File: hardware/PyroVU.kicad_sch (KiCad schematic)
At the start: 48 parts, among them IC1 TM1637__SOP_, J1 Screw_Terminal_01x05, J10 Screw_Terminal_01x09, J11 Screw_Terminal_01x09, J12 Screw_Terminal_01x09, J2 Screw_Terminal_01x02, J3 Conn_01x09_Pin, J4 Conn_01x02_Pin, J5 Conn_01x02_Pin, J6 Conn_01x02_Pin, J7 Screw_Terminal_01x09, J8 Screw_Terminal_01x09, J9 Screw_Terminal_01x09, U1 MAX31856, U3 MAX31865xTP

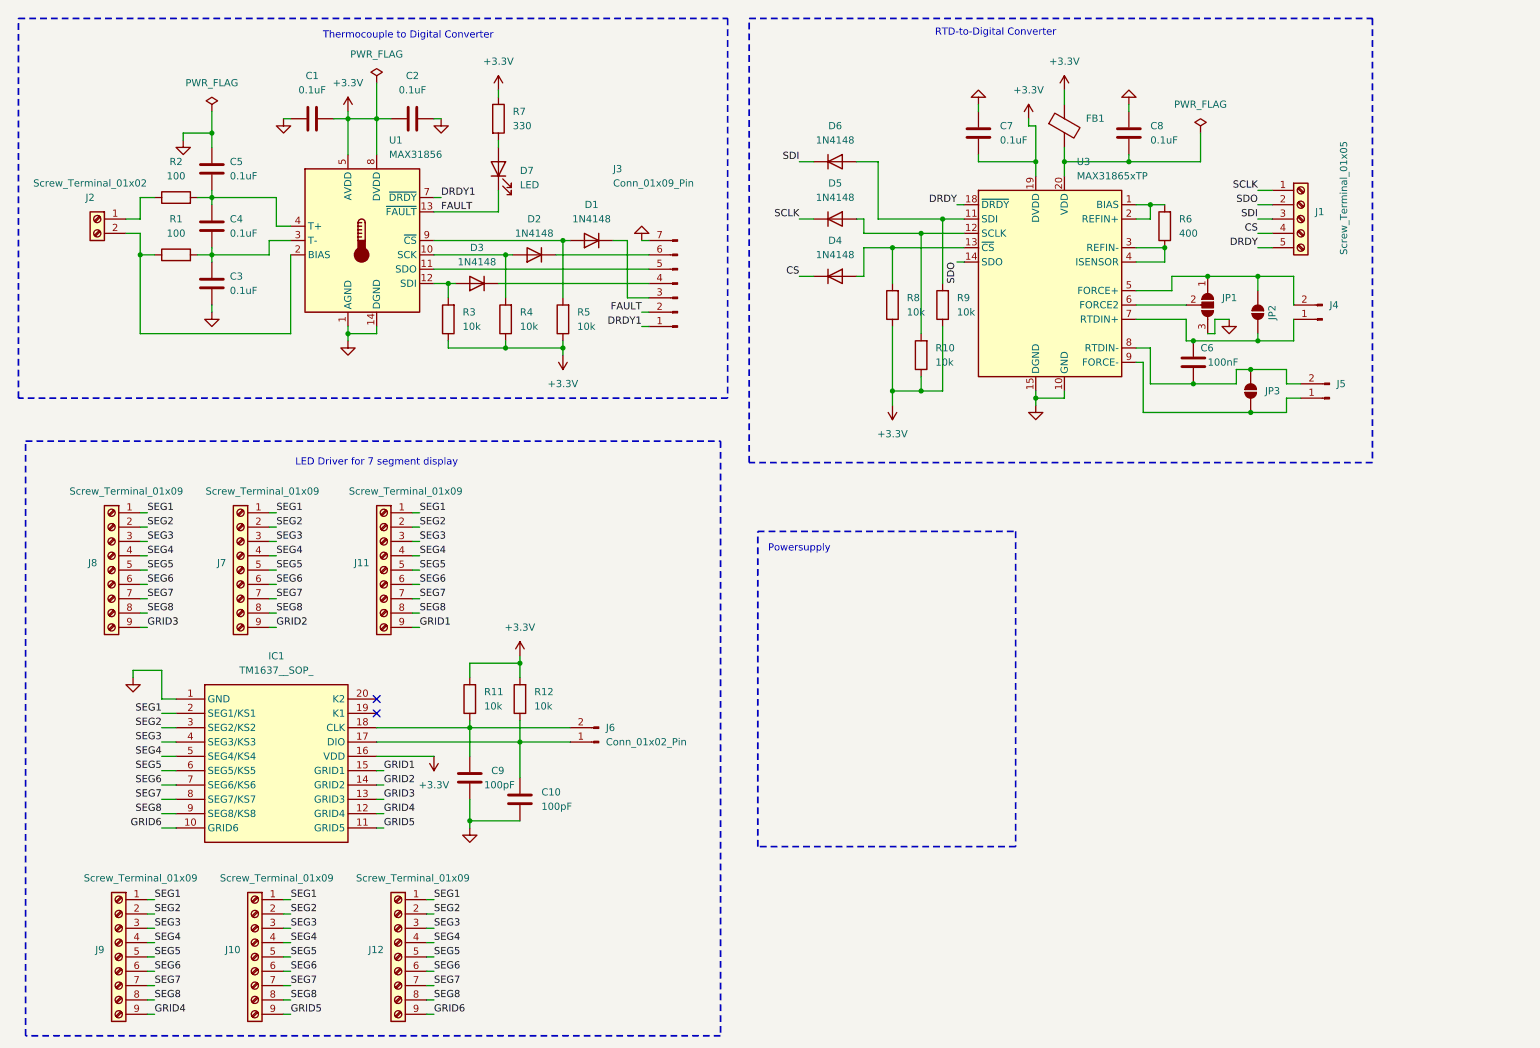
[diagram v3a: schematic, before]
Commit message: Updated the schematic and added 7seg display
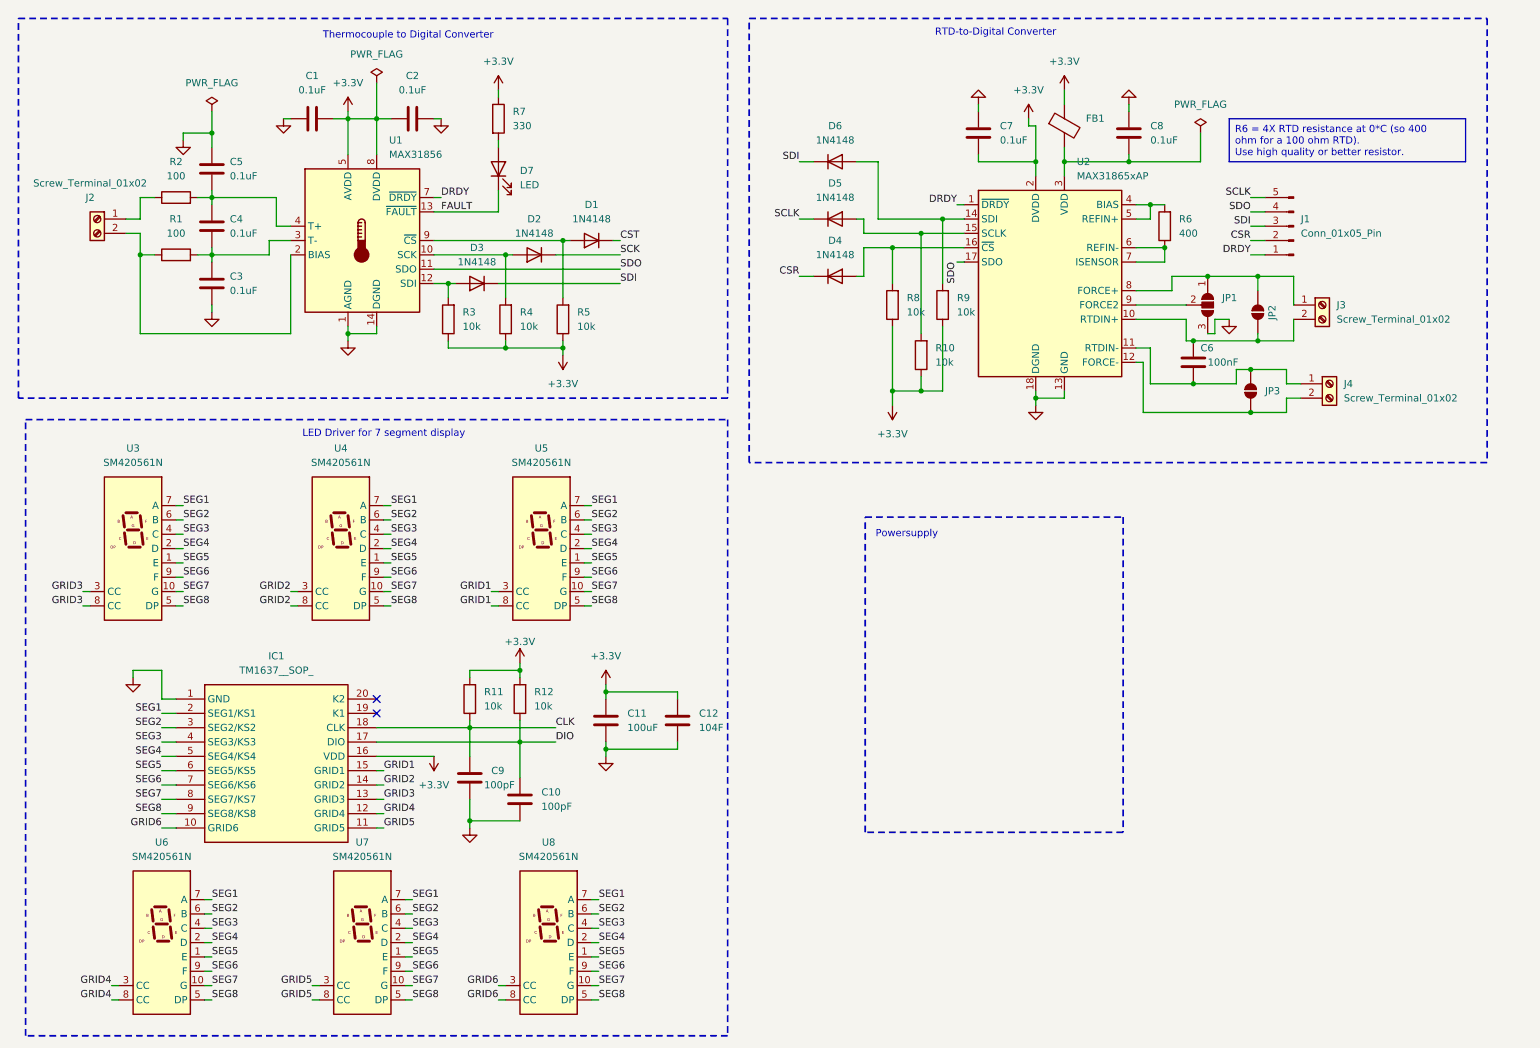
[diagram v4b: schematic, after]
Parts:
- removed J1: Screw_Terminal_01x05, TerminalBlock_Phoenix:TerminalBlock_Phoenix_MPT-0,5-5-2.54_1x05_P2.54mm_Horizontal, symbol Connector:Screw_Terminal_01x05
- removed J10, J11, J12, J7, J8, J9: Screw_Terminal_01x09, TerminalBlock_Phoenix:TerminalBlock_Phoenix_MPT-0,5-9-2.54_1x09_P2.54mm_Horizontal, symbol Connector:Screw_Terminal_01x09
- removed J3: Conn_01x09_Pin, Connector_Molex:Molex_KK-254_AE-6410-07A_1x07_P2.54mm_Vertical, symbol Connector:Conn_01x07_Pin
- removed J4, J5, J6: Conn_01x02_Pin, Connector_Molex:Molex_KK-254_AE-6410-02A_1x02_P2.54mm_Vertical, symbol Connector:Conn_01x02_Pin
- removed U3: MAX31865xTP, Package_DFN_QFN:TQFN-20-1EP_5x5mm_P0.65mm_EP3.25x3.25mm, symbol Sensor_Temperature:MAX31865xTP
- added C11: 100uF, symbol Device:C
- added C12: 104F, symbol Device:C
- added J1: Conn_01x05_Pin, symbol Connector:Conn_01x05_Pin
- added J3, J4: Screw_Terminal_01x02, symbol Connector:Screw_Terminal_01x02
- added U2: MAX31865xAP, Package_SO:SSOP-20_5.3x7.2mm_P0.65mm, symbol Sensor_Temperature:MAX31865xAP
- added U3, U4, U5, U6, U7, U8: SM420561N, Display_7Segment:7SegmentLED_LTS6760_LTS6780, symbol Display_Character:SM420561N
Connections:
- net DRDY1 is gone; now on net DRDY: U1.7 (~{DRDY})
- net +3.3V: now also C11.1, C12.1, U2.2 (DVDD)
- net DRDY: now also J1.1 (Pin_1), U2.1 (~{DRDY})
- net GND: now also C11.2, C12.2, U2.13 (GND), U2.18 (DGND), U2.19 (GND)
- net GRID1: now also U5.3 (CC), U5.8 (CC)
- net GRID2: now also U4.3 (CC), U4.8 (CC)
- net GRID3: now also U3.3 (CC), U3.8 (CC)
- net GRID4: now also U6.3 (CC), U6.8 (CC)
- net GRID5: now also U7.3 (CC), U7.8 (CC)
- net GRID6: now also U8.3 (CC), U8.8 (CC)
- net SCLK: now also J1.5 (Pin_5)
- net SDI: now also D3.1 (K), J1.3 (Pin_3)
- net SDO: now also U1.11 (SDO), J1.4 (Pin_4), U2.17 (SDO)
- net SEG1: now also U3.7 (A), U4.7 (A), U5.7 (A), U6.7 (A), U7.7 (A), U8.7 (A)
- net SEG2: now also U3.6 (B), U4.6 (B), U5.6 (B), U6.6 (B), U7.6 (B), U8.6 (B)
- net SEG3: now also U3.4 (C), U4.4 (C), U5.4 (C), U6.4 (C), U7.4 (C), U8.4 (C)
- net SEG4: now also U3.2 (D), U4.2 (D), U5.2 (D), U6.2 (D), U7.2 (D), U8.2 (D)
- net SEG5: now also U3.1 (E), U4.1 (E), U5.1 (E), U6.1 (E), U7.1 (E), U8.1 (E)
- net SEG6: now also U3.9 (F), U4.9 (F), U5.9 (F), U6.9 (F), U7.9 (F), U8.9 (F)
- net SEG7: now also U3.10 (G), U4.10 (G), U5.10 (G), U6.10 (G), U7.10 (G), U8.10 (G)
- net SEG8: now also U3.5 (DP), U4.5 (DP), U5.5 (DP), U6.5 (DP), U7.5 (DP), U8.5 (DP)
- net at C6.1, JP2.1 (A): now also J3.2 (Pin_2), U2.10 (RTDIN+)
- net at JP1.1 (A), JP2.2 (B): now also J3.1 (Pin_1), U2.8 (FORCE+)
- net at D6.2 (A), R9.2: now also U2.14 (SDI)
- net at D4.2 (A), R8.2: now also U2.16 (~{CS})
- net at JP3.1 (A): now also J4.2 (Pin_2), U2.12 (FORCE-)
- net at C6.2, JP3.2 (B): now also J4.1 (Pin_1), U2.11 (RTDIN-)
- net at C8.2, FB1.2: now also U2.3 (VDD)
- net CST: now reaches D1.1 (K)
- net at D5.2 (A), R10.2: now also U2.15 (SCLK)
- net at JP1.2 (C): now also U2.9 (FORCE2)
- net CLK: now reaches C9.2, IC1.18 (CLK), R11.1
- net SCK: now reaches D2.1 (K)
- net DIO: now reaches C10.2, IC1.17 (DIO), R12.1
- net at R6.1: now also U2.6 (REFIN-), U2.7 (ISENSOR)
- net at R6.2: now also U2.4 (BIAS), U2.5 (REFIN+)
- net CS renamed CSR
- net CSR: now also J1.2 (Pin_2)

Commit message: Changes in the Schematic
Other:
- moved on the sheet: C1, C10, C11, C12, C2, C3, C4, C5, C6, C7, C8, C9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
